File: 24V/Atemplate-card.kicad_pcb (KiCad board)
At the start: 2 copper layers, 111.8 x 83 mm, 3 parts, among them J1 Conn_01x10_Pin, SW1 SW_DPDT_x2

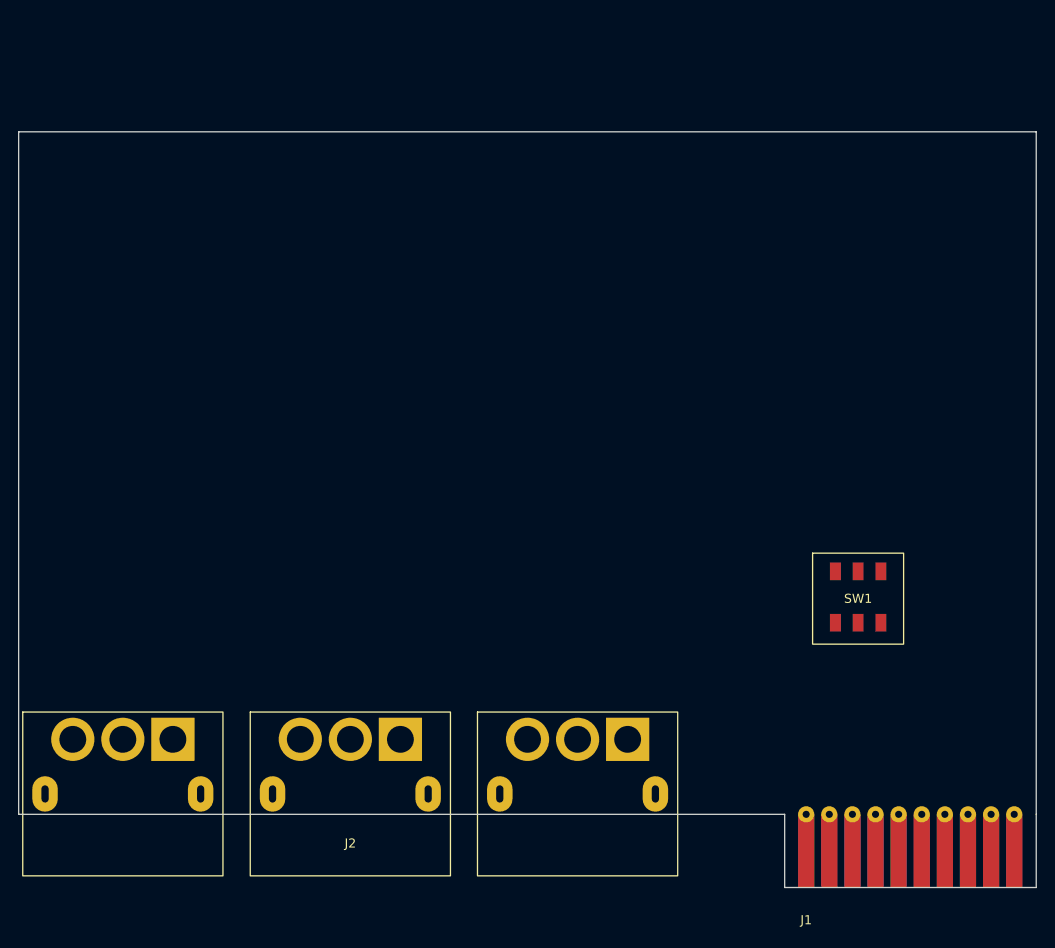
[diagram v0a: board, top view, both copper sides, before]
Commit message: Designed the 5v voltage regulator
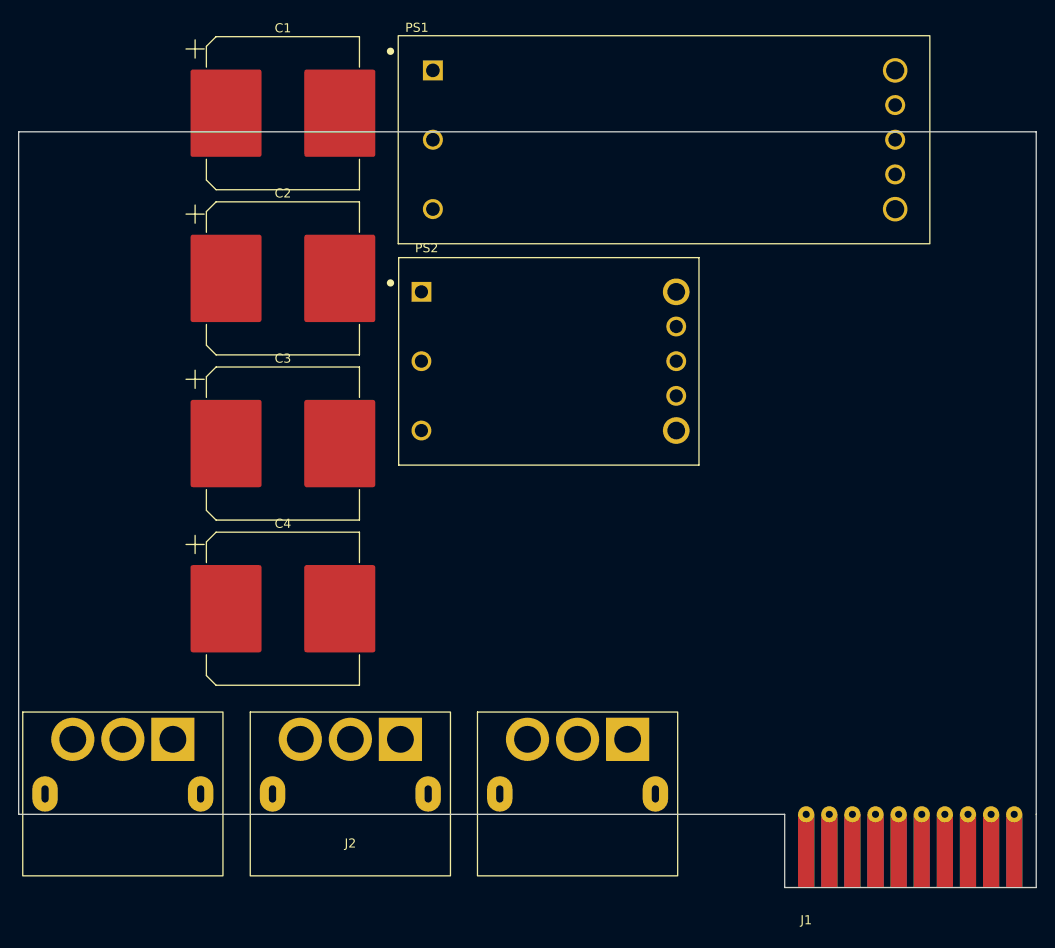
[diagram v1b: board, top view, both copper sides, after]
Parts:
- removed SW1: SW_DPDT_x2, 2024-backplane:SW_CUI_DPDT
- added C1: 100uF/100v, Capacitor_SMD:CP_Elec_16x17.5, F.Cu at (114.7, 23.0)
- added C2: 470uF/50v, Capacitor_SMD:CP_Elec_16x17.5, F.Cu at (114.7, 41.1)
- added C3: 470uF/50v, Capacitor_SMD:CP_Elec_16x17.5, F.Cu at (114.7, 59.3)
- added C4: 470uF/50v, Capacitor_SMD:CP_Elec_16x17.5, F.Cu at (114.7, 77.4)
- added PS1: VCF4824EBO-75WFR3-N, 2024-power:Mornsun VCF4824EBO-75WFR3-N, F.Cu at (127.4, 37.3)
- added PS2: V36SE05010NRFA, 2024-power:Delta V36SE05010NRFA, F.Cu at (143.9, 50.2)
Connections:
- J1 pad 2: /tx0/sda0 -> unconnected-(J1-TX0/SDA0-Pad2)_1
- J1 pad 3: /rx0/scl0 -> unconnected-(J1-RX0/SCL0-Pad3)_1
- J1 pad 5: /tx1/sda1 -> unconnected-(J1-TX1/SDA1-Pad5)
- J1 pad 6: /rx1/scl1 -> unconnected-(J1-RX1/SCL1-Pad6)
- J1 pad 8: /tx2/sda2 -> unconnected-(J1-TX2/SDA2-Pad8)_1
- J1 pad 9: /rx2/scl2 -> unconnected-(J1-RX2/SCL2-Pad9)_0
- J2 pad 2: /24v -> GND2
- J2 pad 4: /12v -> unconnected-(J2B-12V-Pad4)
- J2 pad 5: /12v -> unconnected-(J2B-12V-Pad5)
- J2 pad 6: /12v -> unconnected-(J2B-12V-Pad6)
- J2 pad 7: GND2 -> /24v
- J2 pad 8: /5v -> GND2
- J2 pad 9: GND2 -> /5v

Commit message: Complete Power Boards
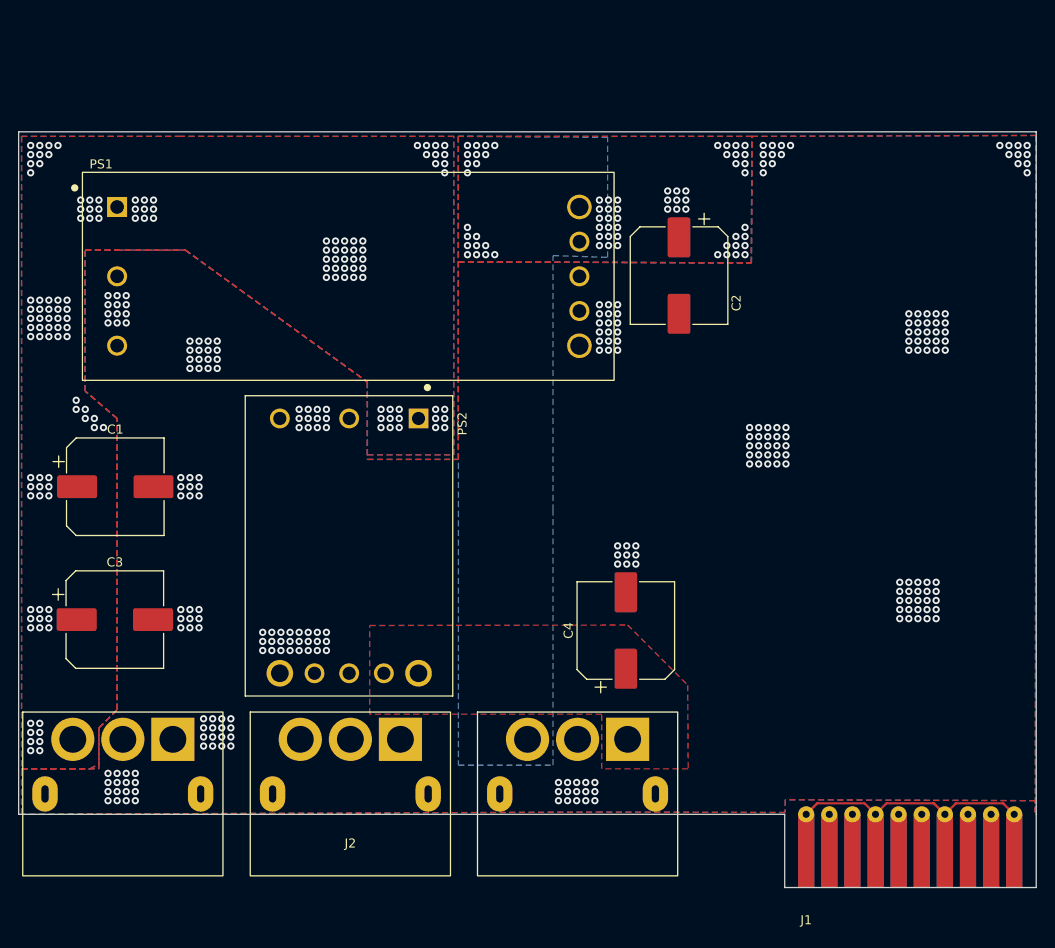
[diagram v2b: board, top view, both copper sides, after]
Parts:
- C1, C2, C4: footprint Capacitor_SMD:CP_Elec_16x17.5 -> Capacitor_SMD:CP_Elec_10x12.5
- C3: value 470uF/50v -> 100uF/100V; footprint Capacitor_SMD:CP_Elec_16x17.5 -> Capacitor_SMD:CP_Elec_10x12.5
- moved C1 45.0 mm to (96.3, 64.0)
- moved C2 43.5 mm to (158.2, 40.8), turned to -90 degrees
- moved PS1 37.8 mm to (92.7, 52.3)
- moved C4 37.8 mm to (152.4, 79.8), turned to 90 degrees
- moved PS2 29.9 mm to (122.0, 70.5), turned to -90 degrees
- moved C3 26.7 mm to (96.2, 78.6)
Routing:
- net GND1: track 0.00 -> 25.9 mm
- net GND2: vias 0 -> 251
- net /48v: vias 0 -> 136
- net /24v: vias 0 -> 67
- added copper zone on B.Cu, net /24v
- added copper zone on F.Cu, net /24v
- added copper zone on B.Cu, net /48v
- added copper zone on F.Cu, net /48v
- added copper zone on F.Cu, net /5v
- added copper zone on B.Cu, net GND2
- added copper zone on F.Cu, net GND2
